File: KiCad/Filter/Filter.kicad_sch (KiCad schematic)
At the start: 25 parts, among them U7 TL074, U8 TL074

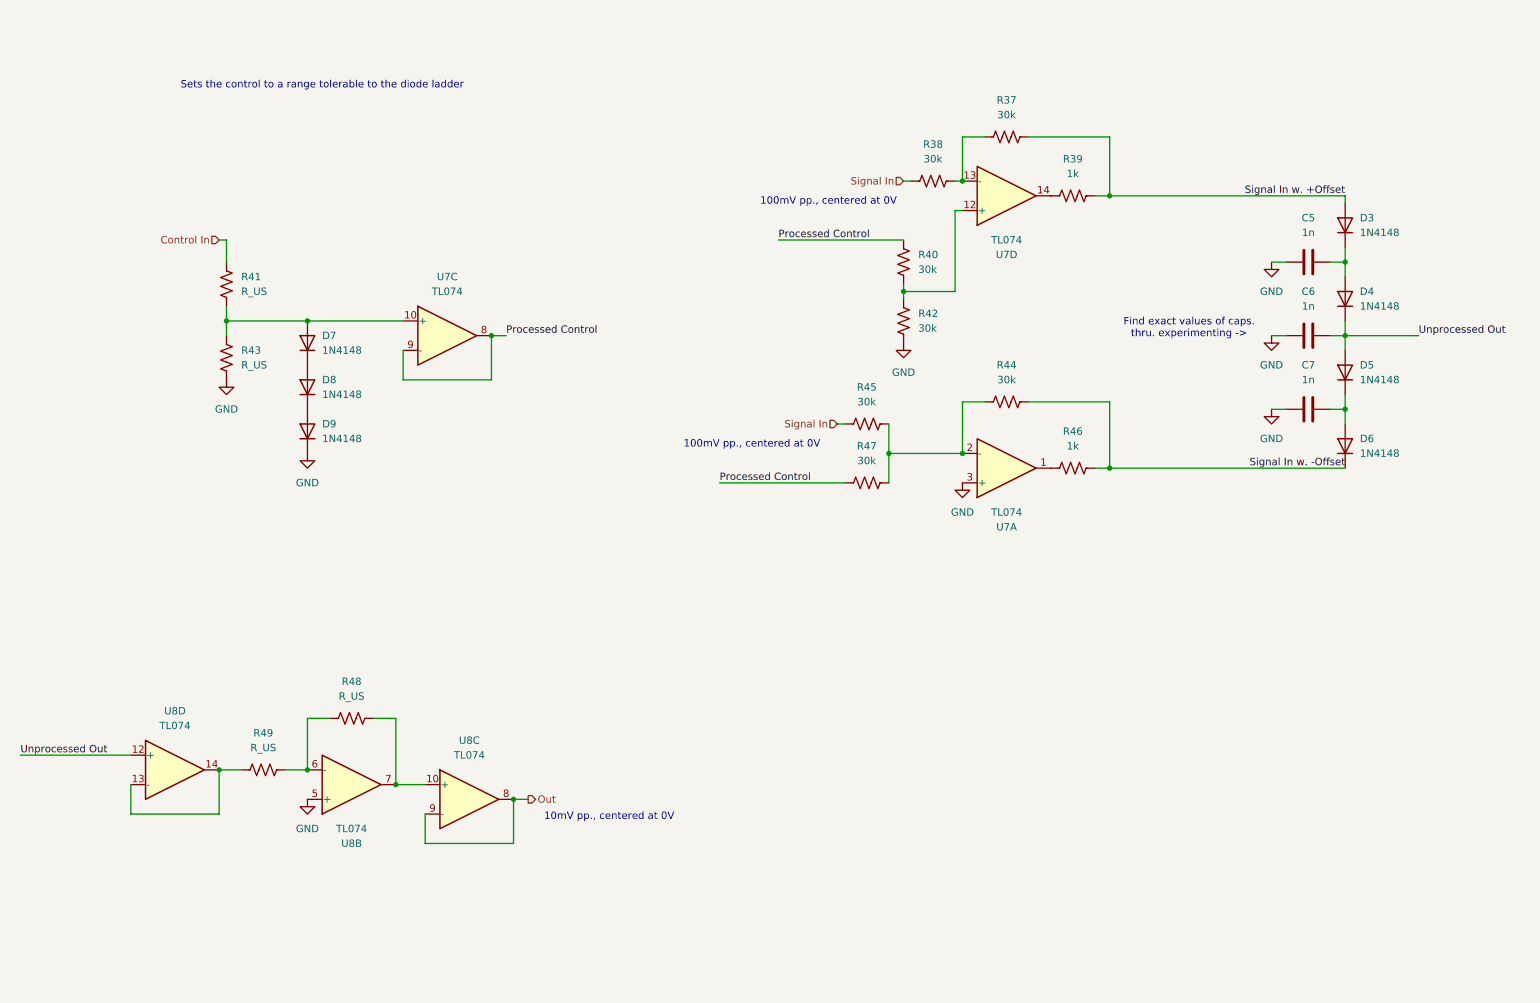
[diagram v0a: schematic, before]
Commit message: started separating into different boards, partially fixed envelope generator
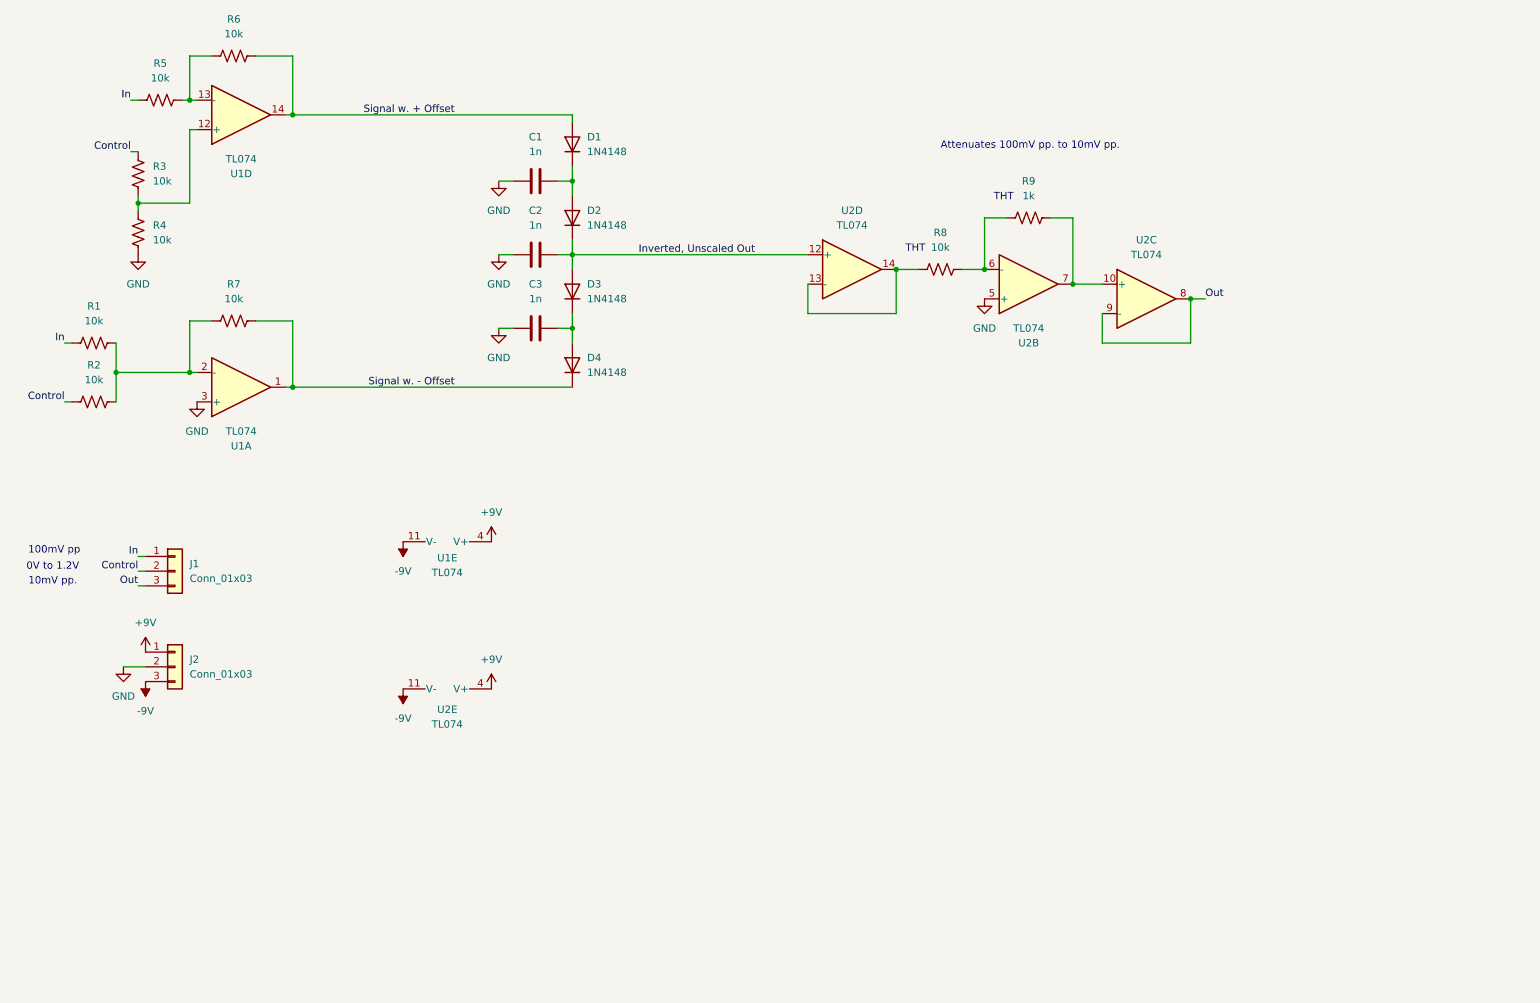
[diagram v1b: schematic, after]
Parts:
- removed D7, D8, D9: 1N4148, Diode_THT:D_DO-35_SOD27_P7.62mm_Horizontal, symbol Diode:1N4148
- removed R39, R46: 1k, Resistor_SMD:R_0603_1608Metric, symbol Device:R_US
- removed R41, R43: R_US, Resistor_THT:R_Axial_DIN0207_L6.3mm_D2.5mm_P7.62mm_Horizontal, symbol Device:R_US
- removed unit 3 of U7
- added J1, J2: Conn_01x03, symbol Connector_Generic:Conn_01x03
- added unit 5 of U1
- added unit 5 of U2
- R1: renamed from R45; value 30k -> 10k
- R2: renamed from R47; value 30k -> 10k
- R3: renamed from R40; value 30k -> 10k
- R4: renamed from R42; value 30k -> 10k
- R5: renamed from R38; value 30k -> 10k
- R6: renamed from R37; value 30k -> 10k
- R7: renamed from R44; value 30k -> 10k
- R8: renamed from R49; value R_US -> 10k
- R9: renamed from R48; value R_US -> 1k
- renumbered C5 to C1, C6 to C2, C7 to C3, D3 to D1, D4 to D2, D5 to D3, D6 to D4, U7 to U1, U8 to U2
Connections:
- net Signal In w. +Offset is gone; now on net Signal w. + Offset: D1.2 (A), R6.2
- net Signal In w. -Offset is gone; now on net Signal w. - Offset: D4.1 (K), R7.2
- net GND: now also J2.2 (Pin_2)
- net Out: now also J1.3 (Pin_3)
- net Signal w. - Offset: now reaches U1.1
- net Signal w. + Offset: now reaches U1.14
- net Processed Control renamed Control
- net Control: now also J1.2 (Pin_2)
- net Signal In renamed In
- net In: now also J1.1 (Pin_1)
- net Unprocessed Out renamed Inverted, Unscaled Out
- new net +9V: J2.1 (Pin_1), U1.4 (V+), U2.4 (V+)
- new net -9V: J2.3 (Pin_3), U1.11 (V-), U2.11 (V-)
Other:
- note added: "0V to 1.2V"
- note added: "100mV pp"
- note added: "10mV pp."
- note added: "Attenuates 100mV pp. to 10mV pp."
- note added: "THT"
- note removed: "100mV pp., centered at 0V"
- note removed: "10mV pp., centered at 0V"
- note removed: "Find exact values of caps. thru. experimenting ->"
- note removed: "Sets the control to a range tolerable to the diode ladder"
- moved on the sheet: C1, C2, C3, D1, D2, D3, D4, R1, R2, R3, R4, R5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

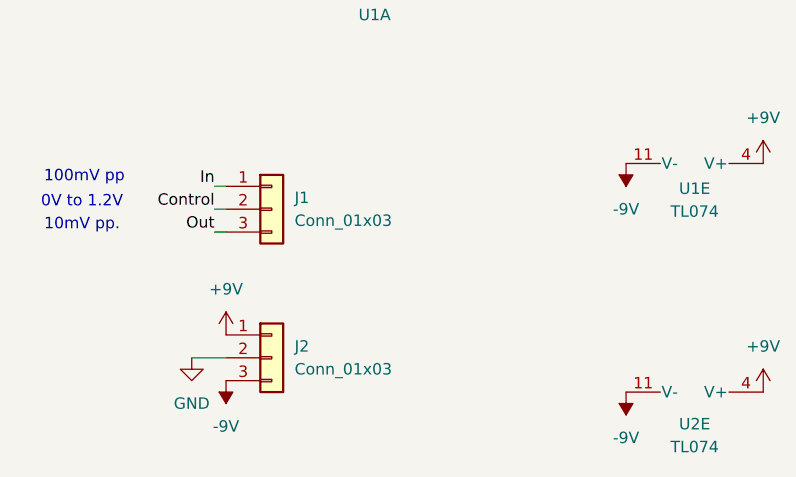
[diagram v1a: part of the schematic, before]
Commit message: fixed power board, replaced sketchy voltage divider - op amp cct. with an LDO to product +5V
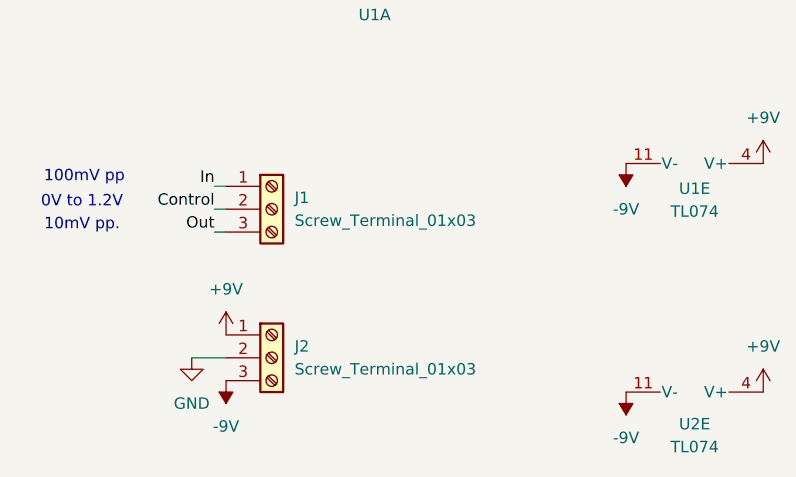
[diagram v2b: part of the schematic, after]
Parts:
- removed J1, J2: Conn_01x03, symbol Connector_Generic:Conn_01x03
- added J1, J2: Screw_Terminal_01x03, symbol Connector:Screw_Terminal_01x03
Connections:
- net +9V: now also J2.1 (Pin_1)
- net -9V: now also J2.3 (Pin_3)
- net Control: now also J1.2 (Pin_2)
- net GND: now also J2.2 (Pin_2)
- net In: now also J1.1 (Pin_1)
- net Out: now also J1.3 (Pin_3)
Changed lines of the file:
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@@
-	)
-	(symbol
-		(lib_id "Connector_Generic:Conn_01x03")
-		(at 45.72 134.62 0)
-		(unit 1)
-		(body_style 1)
-		(exclude_from_sim no)
-		(in_bom yes)
-		(on_board yes)
-		(in_pos_files yes)
-		(dnp no)
-		(fields_autoplaced yes)
-		(property "Reference" "J2"
-			(at 48.26 133.3499 0)
-			(show_name no)
-			(do_not_autoplace no)
-			(effects
-				(font
-					(size 1.27 1.27)
-				)
-				(justify left)
-			)
-		)
-		(property "Value" "Conn_01x03"
-			(at 48.26 135.8899 0)
-			(show_name no)
-			(do_not_autoplace no)
-			(effects
-				(font
-					(size 1.27 1.27)
-				)
-				(justify left)
-			)
-		)
-		(property "Footprint" ""
-			(at 45.72 134.62 0)
-			(hide yes)
-			(show_name no)
-			(do_not_autoplace no)
-			(effects
-				(font
-					(size 1.27 1.27)
-				)
-			)
-		)
-		(property "Datasheet" ""
-			(at 45.72 134.62 0)
-			(hide yes)
-			(show_name no)
-			(do_not_autoplace no)
-			(effects
-				(font
-					(size 1.27 1.27)
-				)
-			)
-		)
-		(property "Description" "Generic connector, single row, 01x03, script generated (kicad-library-utils/schlib/autogen/connector/)"
-			(at 45.72 134.62 0)
-			(hide yes)
-			(show_name no)
-			(do_not_autoplace no)
-			(effects
-				(font
-					(size 1.27 1.27)
-				)
-			)
-		)
-		(pin "3"
-		)
-		(pin "2"
-		)
-		(pin "1"
-		)
-		(instances
-			(project "Filter"
-				(path "/d0463ce5-c32c-4d9a-94ac-2a0e117a03ce"
-					(reference "J2")
-					(unit 1)
-				)
-			)
-		)
 	)
 	(symbol
@@
 	)
 	(symbol
-		(lib_id "Connector_Generic:Conn_01x03")
+		(lib_id "Connector:Screw_Terminal_01x03")
 		(at 45.72 118.11 0)
 		(unit 1)
@@
 			)
 		)
-		(property "Value" "Conn_01x03"
+		(property "Value" "Screw_Terminal_01x03"
 			(at 48.26 119.3799 0)
 			(show_name no)
@@
 			)
 		)
-		(property "Description" "Generic connector, single row, 01x03, script generated (kicad-library-utils/schlib/autogen/connector/)"
+		(property "Description" "Generic screw terminal, single row, 01x03, script generated (kicad-library-utils/schlib/autogen/connector/)"
 			(at 45.72 118.11 0)
 			(hide yes)
@@
 					(unit 1)
 				)
+			)
+		)
+	)
+	(symbol
+		(lib_id "Connector:Screw_Terminal_01x03")
+		(at 45.72 134.62 0)
+		(unit 1)
+		(body_style 1)
+		(exclude_from_sim no)
+		(in_bom yes)
+		(on_board yes)
+		(in_pos_files yes)
+		(dnp no)
+		(fields_autoplaced yes)
+		(property "Reference" "J2"
+			(at 48.26 133.3499 0)
+			(show_name no)
+			(do_not_autoplace no)
+			(effects
+				(font
+					(size 1.27 1.27)
+				)
+				(justify left)
+			)
+		)
+		(property "Value" "Screw_Terminal_01x03"
+			(at 48.26 135.8899 0)
+			(show_name no)
+			(do_not_autoplace no)
+			(effects
+				(font
+					(size 1.27 1.27)
+				)
+				(justify left)
+			)
+		)
+		(property "Footprint" ""
+			(at 45.72 134.62 0)
+			(hide yes)
+			(show_name no)
+			(do_not_autoplace no)
+			(effects
+				(font
+					(size 1.27 1.27)
+				)
+			)
+		)
+		(property "Datasheet" ""
+			(at 45.72 134.62 0)
+			(hide yes)
+			(show_name no)
+			(do_not_autoplace no)
+			(effects
+				(font
+					(size 1.27 1.27)
+				)
+			)
+		)
+		(property "Description" "Generic screw terminal, single row, 01x03, script generated (kicad-library-utils/schlib/autogen/connector/)"
+			(at 45.72 134.62 0)
+			(hide yes)
+			(show_name no)
+			(do_not_autoplace no)
+			(effects
+				(font
+					(size 1.27 1.27)
+				)
+			)
+		)
+		(pin "3"
+		)
+		(pin "2"
+		)
+		(pin "1"
+		)
+		(instances
+			(project "Filter"
+				(path "/d0463ce5-c32c-4d9a-94ac-2a0e117a03ce"
+					(reference "J2")
+					(unit 1)
+				)

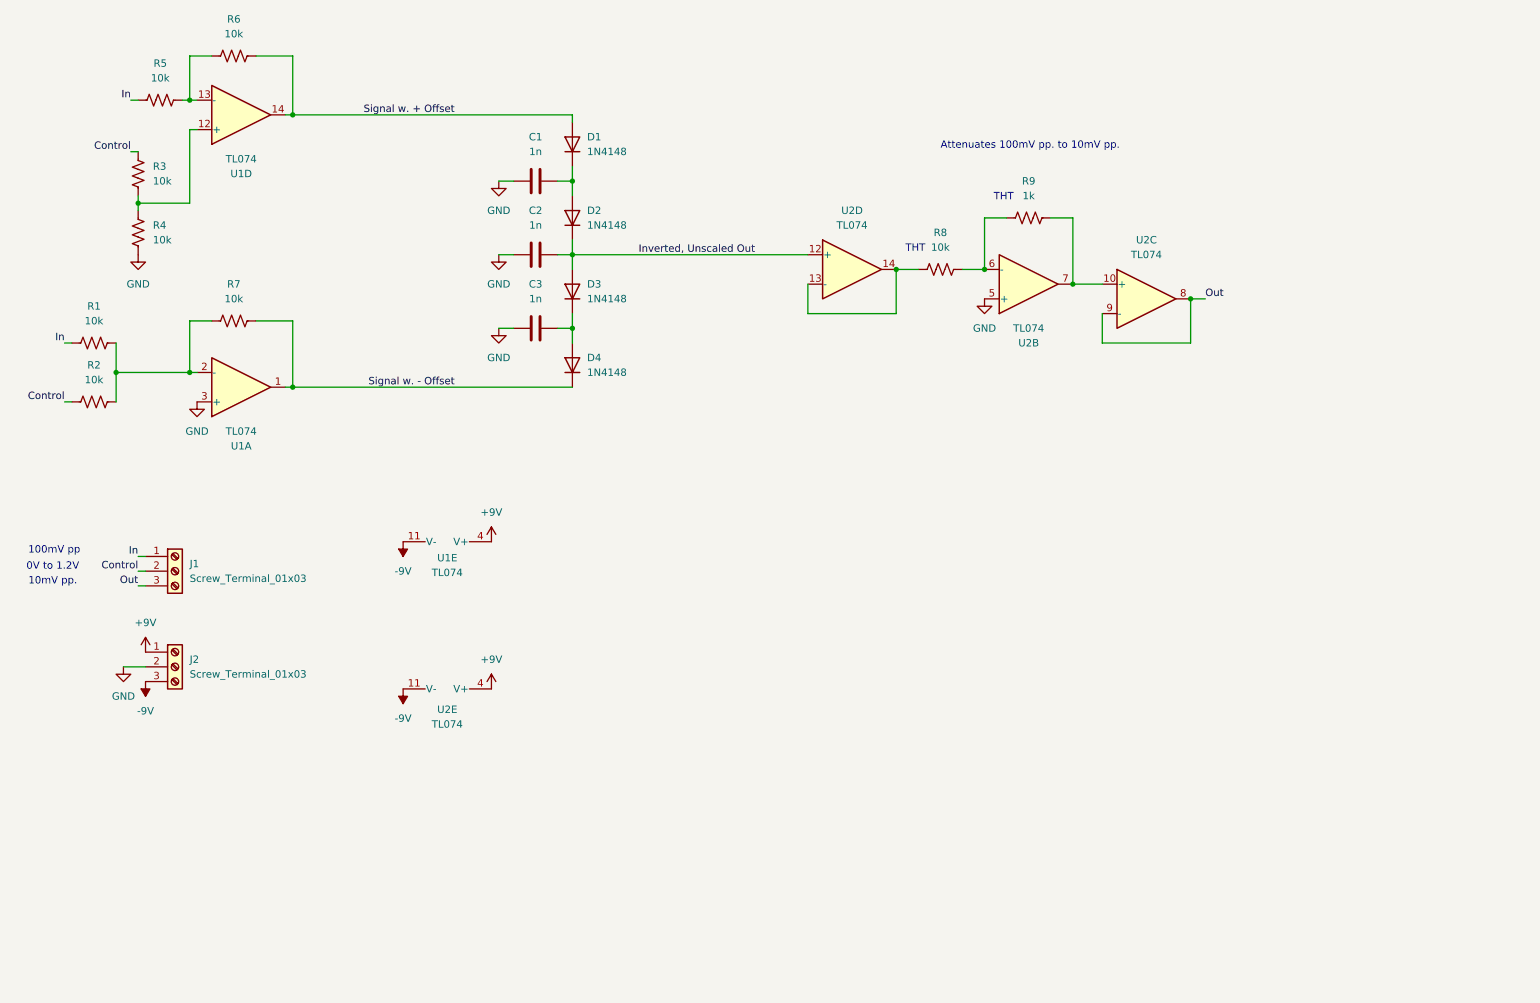
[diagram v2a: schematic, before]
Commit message: finished separating into separate kicad projects
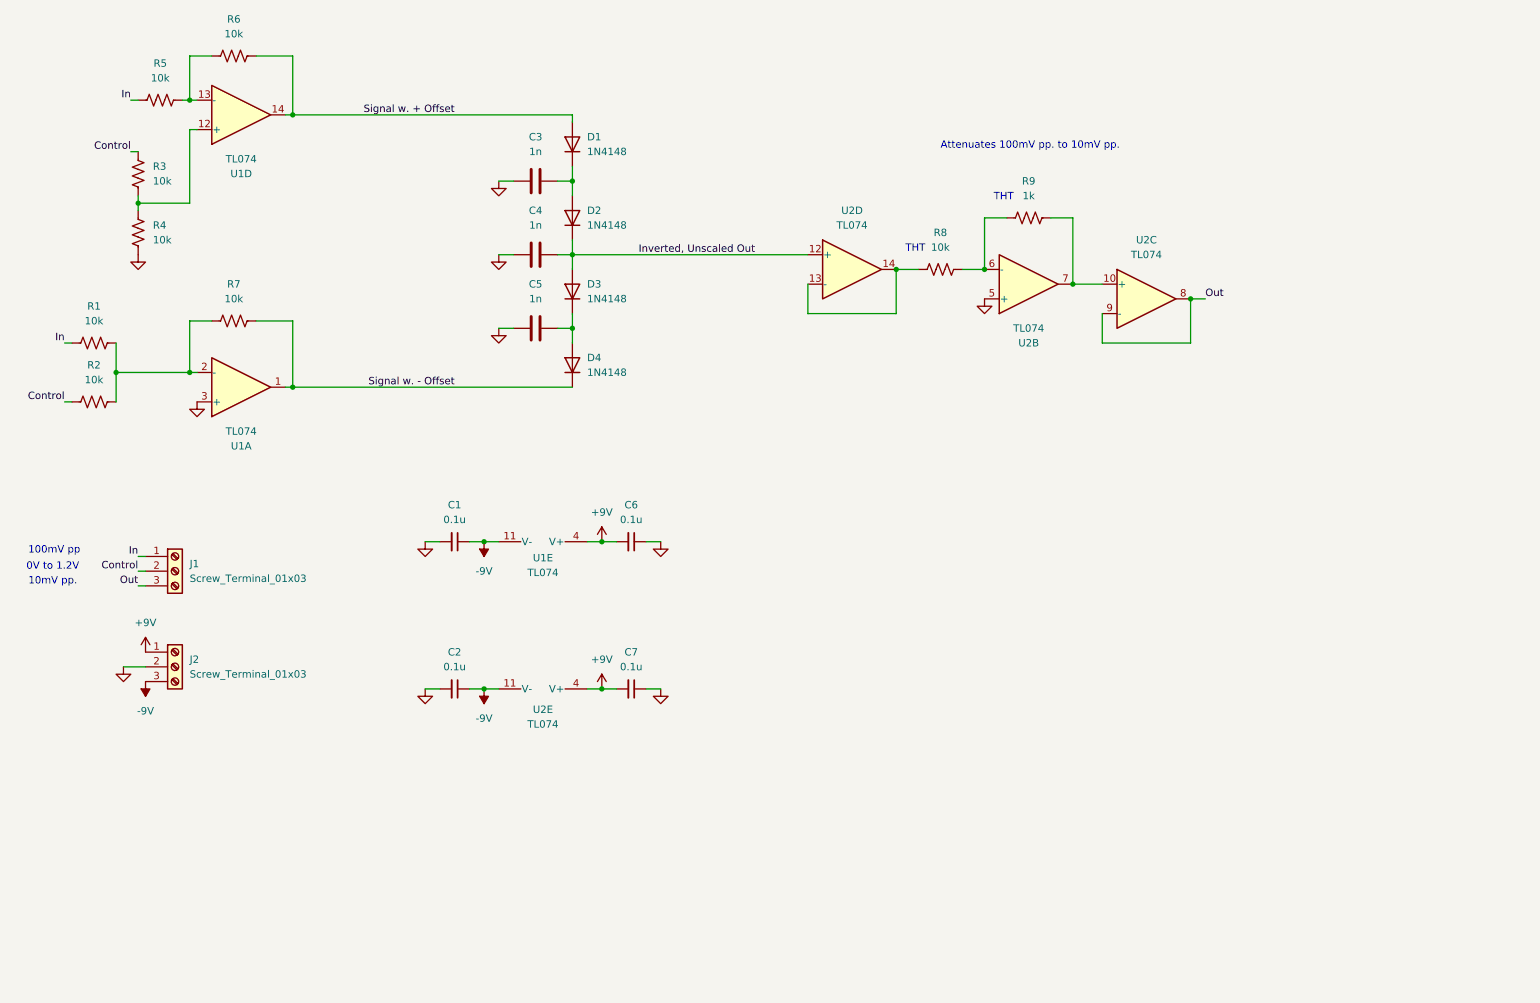
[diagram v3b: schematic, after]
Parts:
- added C1, C2, C6, C7: 0.1u, symbol Device:C_Small
- renumbered C1 to C3, C2 to C4, C3 to C5
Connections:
- net +9V: now also C6.2, C7.2
- net -9V: now also C1.1, C2.1
- net GND: now also C1.2, C2.2, C6.1, C7.1
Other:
- moved on the sheet: U1E, U2E

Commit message: added test points
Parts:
- added TP? (x7): TestPoint_Small, symbol Connector:TestPoint_Small
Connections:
- net Control: now also TP?.1
- net GND: now also TP?.1
- net In: now also TP?.1
- net Inverted, Unscaled Out: now also TP?.1
- net Out: now also TP?.1
- net Signal w. + Offset: now also TP?.1
- net Signal w. - Offset: now also TP?.1
